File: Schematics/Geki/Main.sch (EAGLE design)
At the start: 17 parts

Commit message: fixes, cleanup, new schematics, new 3d files, readme edits, fixes on scripts
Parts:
- removed BUTTONS: (no value), SparkFun-Connectors:CONN_06SILK_FEMALE_PTH
- removed R7, R8, R9: 1k, SparkFun-Resistors:1KOHM-HORIZ-1/4W-1%
- added J1: (no value), SparkFun-Connectors:CONN_04
- added R10: 10k, SparkFun-Resistors:1KOHM-HORIZ-1/4W-1%
- R4, R5, R6: value 1k -> 10k
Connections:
- removed net BTN_5: R5.2, U$1.GEN/6GPIO25
- removed net BTN_6: R4.2, U$1.!CE0!/GPIO8
- removed net N$10: BUTTONS.3, R7.1
- removed net N$11: BUTTONS.2, R8.1
- removed net N$12: BUTTONS.1, R9.1
- removed net N$7: BUTTONS.6, R4.1
- removed net N$8: BUTTONS.5, R5.1
- removed net N$9: BUTTONS.4, R6.1
- net BTN_1: now also J1.1, R10.1; no longer R9.2
- net BTN_2: now also J1.2, R4.1; no longer R8.2
- net BTN_3: now also J1.3, R5.1; no longer R7.2
- net BTN_4: now also J1.4, R6.1; no longer R6.2
- net GND-ISO: now also R10.2, R4.2, R5.2, R6.2
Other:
- moved on the sheet: R4, R5, R6

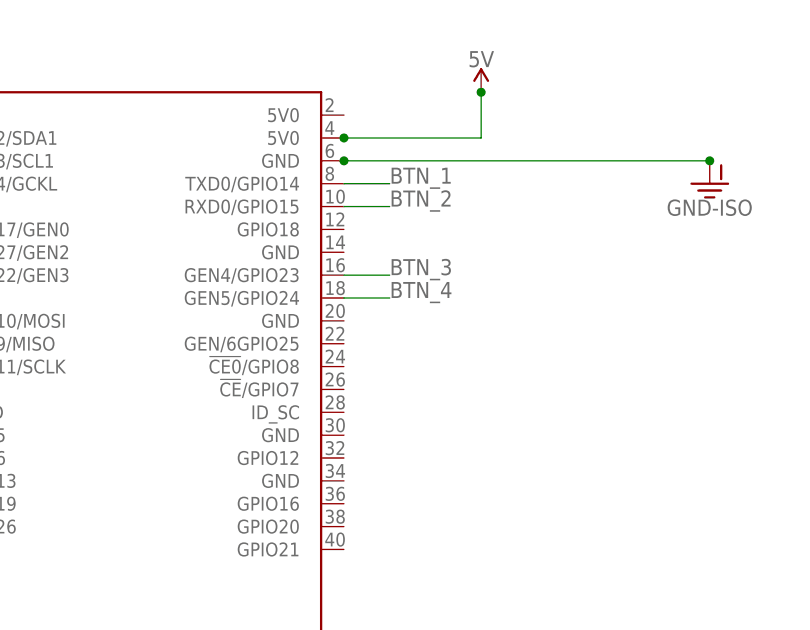
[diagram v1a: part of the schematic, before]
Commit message: new schematic fixes and install script fix
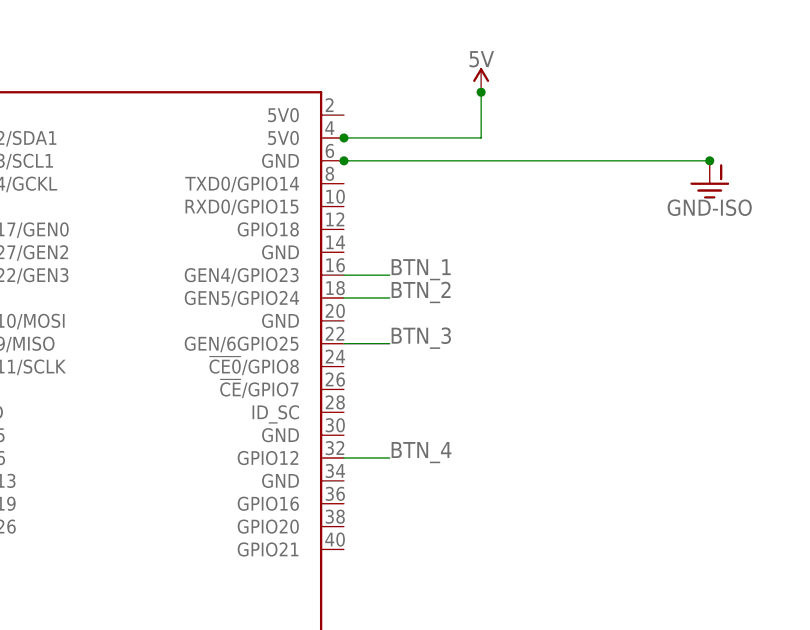
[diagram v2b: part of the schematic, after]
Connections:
- net BTN_1: now also U$1.GEN4/GPIO23; no longer U$1.TXD0/GPIO14
- net BTN_2: now also U$1.GEN5/GPIO24; no longer U$1.RXD0/GPIO15
- net BTN_3: now also U$1.GEN/6GPIO25; no longer U$1.GEN4/GPIO23
- net BTN_4: now also U$1.GPIO12; no longer U$1.GEN5/GPIO24
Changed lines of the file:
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@@
 <net name="BTN_3" class="0">
-<segment>
-<pinref part="U$1" gate="G$1" pin="GEN4/GPIO23"/>
-<wire x1="129.54" y1="58.42" x2="134.62" y2="58.42" width="0.1524" layer="91"/>
-<label x="134.62" y="58.42" size="1.778" layer="95"/>
-</segment>
 <segment>
 <pinref part="J1" gate="G$1" pin="3"/>
@@
 <label x="10.16" y="5.08" size="1.778" layer="95"/>
 </segment>
+<segment>
+<pinref part="U$1" gate="G$1" pin="GEN/6GPIO25"/>
+<wire x1="129.54" y1="50.8" x2="134.62" y2="50.8" width="0.1524" layer="91"/>
+<label x="134.62" y="50.8" size="1.778" layer="95"/>
+</segment>
 </net>
 <net name="BTN_4" class="0">
-<segment>
-<pinref part="U$1" gate="G$1" pin="GEN5/GPIO24"/>
-<wire x1="129.54" y1="55.88" x2="134.62" y2="55.88" width="0.1524" layer="91"/>
-<label x="134.62" y="55.88" size="1.778" layer="95"/>
-</segment>
 <segment>
 <pinref part="J1" gate="G$1" pin="4"/>
@@
 <label x="10.16" y="7.62" size="1.778" layer="95"/>
 </segment>
+<segment>
+<pinref part="U$1" gate="G$1" pin="GPIO12"/>
+<wire x1="129.54" y1="38.1" x2="134.62" y2="38.1" width="0.1524" layer="91"/>
+<label x="134.62" y="38.1" size="1.778" layer="95"/>
+</segment>
 </net>
 <net name="BTN_1" class="0">
-<segment>
-<pinref part="U$1" gate="G$1" pin="TXD0/GPIO14"/>
-<wire x1="129.54" y1="68.58" x2="134.62" y2="68.58" width="0.1524" layer="91"/>
-<label x="134.62" y="68.58" size="1.778" layer="95"/>
-</segment>
 <segment>
 <pinref part="J1" gate="G$1" pin="1"/>
@@
 <label x="10.16" y="0" size="1.778" layer="95"/>
 </segment>
+<segment>
+<pinref part="U$1" gate="G$1" pin="GEN4/GPIO23"/>
+<wire x1="129.54" y1="58.42" x2="134.62" y2="58.42" width="0.1524" layer="91"/>
+<label x="134.62" y="58.42" size="1.778" layer="95"/>
+</segment>
 </net>
 <net name="BTN_2" class="0">
-<segment>
-<pinref part="U$1" gate="G$1" pin="RXD0/GPIO15"/>
-<wire x1="129.54" y1="66.04" x2="134.62" y2="66.04" width="0.1524" layer="91"/>
-<label x="134.62" y="66.04" size="1.778" layer="95"/>
-</segment>
 <segment>
 <pinref part="J1" gate="G$1" pin="2"/>
@@
 <label x="10.16" y="2.54" size="1.778" layer="95"/>
 </segment>
+<segment>
+<pinref part="U$1" gate="G$1" pin="GEN5/GPIO24"/>
+<wire x1="129.54" y1="55.88" x2="134.62" y2="55.88" width="0.1524" layer="91"/>
+<label x="134.62" y="55.88" size="1.778" layer="95"/>
+</segment>
 </net>
